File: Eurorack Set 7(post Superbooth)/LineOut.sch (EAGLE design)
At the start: 25 parts, among them IC1 NE5532D

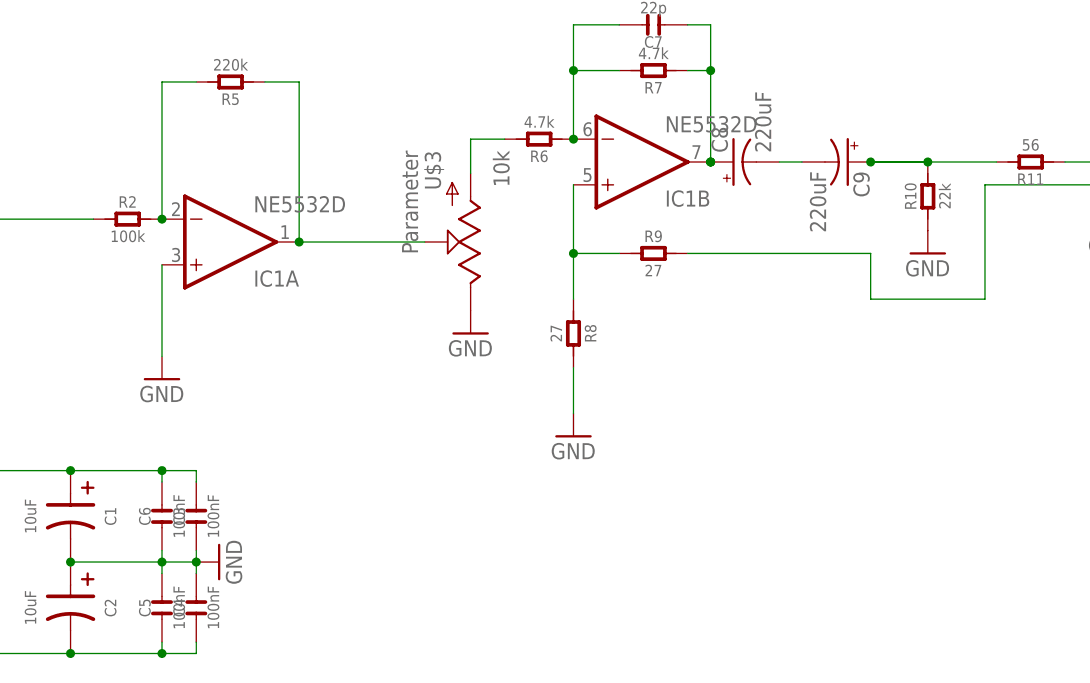
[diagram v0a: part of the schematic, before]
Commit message: EnvFollower values, bigfish fixes, wobbler updates, lineout clarifications
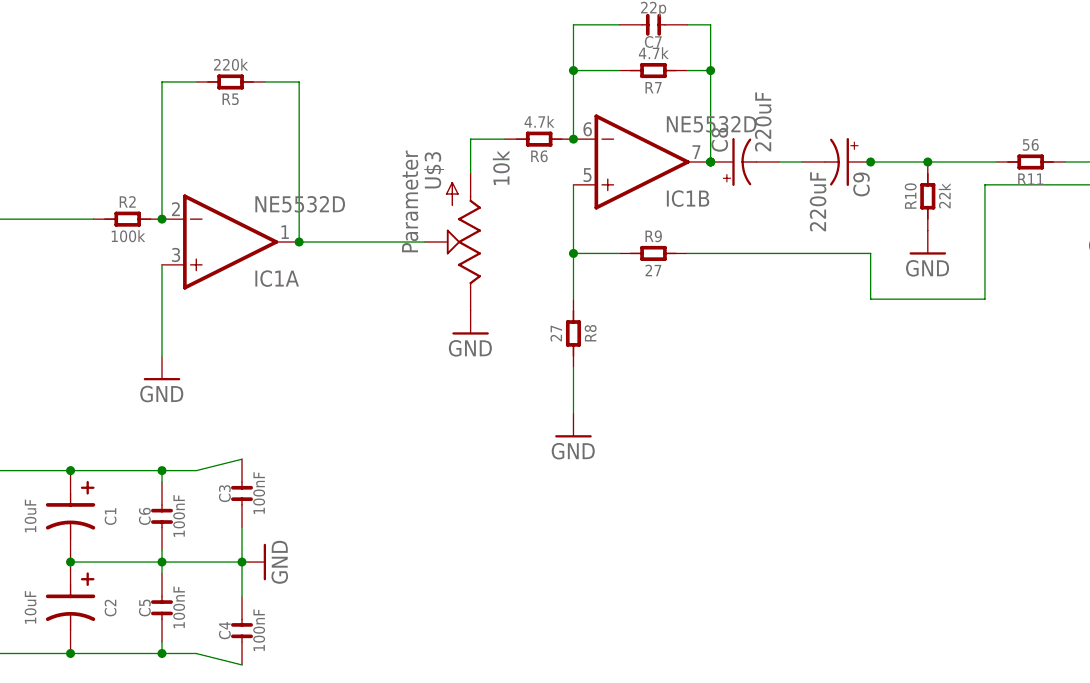
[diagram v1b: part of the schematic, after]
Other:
- moved on the sheet: C3, C4
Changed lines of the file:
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@@
 <setting verticaltext="up"/>
 </settings>
-<grid distance="0.05" unitdist="inch" unit="inch" style="lines" multiple="1" display="no" altdistance="0.01" altunitdist="inch" altunit="inch"/>
+<grid distance="0.1" unitdist="inch" unit="inch" style="lines" multiple="1" display="no" altdistance="0.01" altunitdist="inch" altunit="inch"/>
 <layers>
 <layer number="1" name="Top" color="4" fill="1" visible="no" active="no"/>
@@
 <instance part="U$1" gate="G$1" x="5.08" y="12.7"/>
 <instance part="U$5" gate="G$1" x="1.27" y="55.88"/>
-<instance part="GND1" gate="1" x="52.07" y="12.7" rot="R90"/>
+<instance part="GND1" gate="1" x="57.15" y="12.7" rot="R90"/>
 <instance part="GND2" gate="1" x="91.44" y="26.67"/>
 <instance part="GND3" gate="1" x="45.72" y="33.02"/>
@@
 <instance part="C9" gate="G$1" x="121.92" y="57.15" rot="R270"/>
 <instance part="JP1" gate="G$1" x="184.15" y="54.61" rot="R180"/>
-<instance part="C3" gate="C" x="49.53" y="17.78" rot="R90"/>
-<instance part="C4" gate="C" x="49.53" y="7.62" rot="R90"/>
+<instance part="C3" gate="C" x="54.61" y="20.32" rot="R90"/>
+<instance part="C4" gate="C" x="54.61" y="5.08" rot="R90"/>
 <instance part="GND6" gate="1" x="17.78" y="12.7" rot="R90"/>
 <instance part="JP3" gate="G$1" x="226.06" y="46.99" rot="R180"/>
@@
 <pinref part="C2" gate="C" pin="1"/>
 <pinref part="GND1" gate="1" pin="GND"/>
-<junction x="49.53" y="12.7"/>
-<wire x1="49.53" y1="12.7" x2="45.72" y2="12.7" width="0.1524" layer="91"/>
+<junction x="54.61" y="12.7"/>
+<wire x1="54.61" y1="12.7" x2="45.72" y2="12.7" width="0.1524" layer="91"/>
 <junction x="35.56" y="12.7"/>
 <junction x="45.72" y="12.7"/>
@@
 <wire x1="45.72" y1="13.97" x2="45.72" y2="12.7" width="0.1524" layer="91"/>
 <pinref part="C4" gate="C" pin="2"/>
-<wire x1="49.53" y1="11.43" x2="49.53" y2="12.7" width="0.1524" layer="91"/>
+<wire x1="54.61" y1="8.89" x2="54.61" y2="12.7" width="0.1524" layer="91"/>
 <pinref part="C3" gate="C" pin="1"/>
-<wire x1="49.53" y1="13.97" x2="49.53" y2="12.7" width="0.1524" layer="91"/>
+<wire x1="54.61" y1="16.51" x2="54.61" y2="12.7" width="0.1524" layer="91"/>
 </segment>
 <segment>
@@
 <pinref part="R11" gate="R" pin="2"/>
 <pinref part="R10" gate="R" pin="2"/>
-<wire x1="124.46" y1="57.15" x2="130.81" y2="57.15" width="0.1524" layer="91"/>
 <pinref part="C9" gate="G$1" pin="+"/>
 <junction x="124.46" y="57.15"/>
@@
 <wire x1="15.24" y1="22.86" x2="25.4" y2="22.86" width="0.1524" layer="91"/>
 <pinref part="C3" gate="C" pin="2"/>
-<wire x1="49.53" y1="21.59" x2="49.53" y2="22.86" width="0.1524" layer="91"/>
+<wire x1="54.61" y1="24.13" x2="49.53" y2="22.86" width="0.1524" layer="91"/>
 <wire x1="49.53" y1="22.86" x2="45.72" y2="22.86" width="0.1524" layer="91"/>
 <junction x="45.72" y="22.86"/>
@@
 <pinref part="C4" gate="C" pin="1"/>
 <wire x1="45.72" y1="2.54" x2="49.53" y2="2.54" width="0.1524" layer="91"/>
-<wire x1="49.53" y1="2.54" x2="49.53" y2="3.81" width="0.1524" layer="91"/>
+<wire x1="49.53" y1="2.54" x2="54.61" y2="1.27" width="0.1524" layer="91"/>
 <junction x="45.72" y="2.54"/>
 </segment>
